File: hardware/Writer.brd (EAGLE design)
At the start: 54 x 56 mm, 52 parts, among them CN1 ZX62-B-5PA(11), CN2 TTL-232R-3V3, CN3 WiFi-Header, CN4 SOCKET-HEADER-7614-5002, IC1 ATMEGA32U4AU

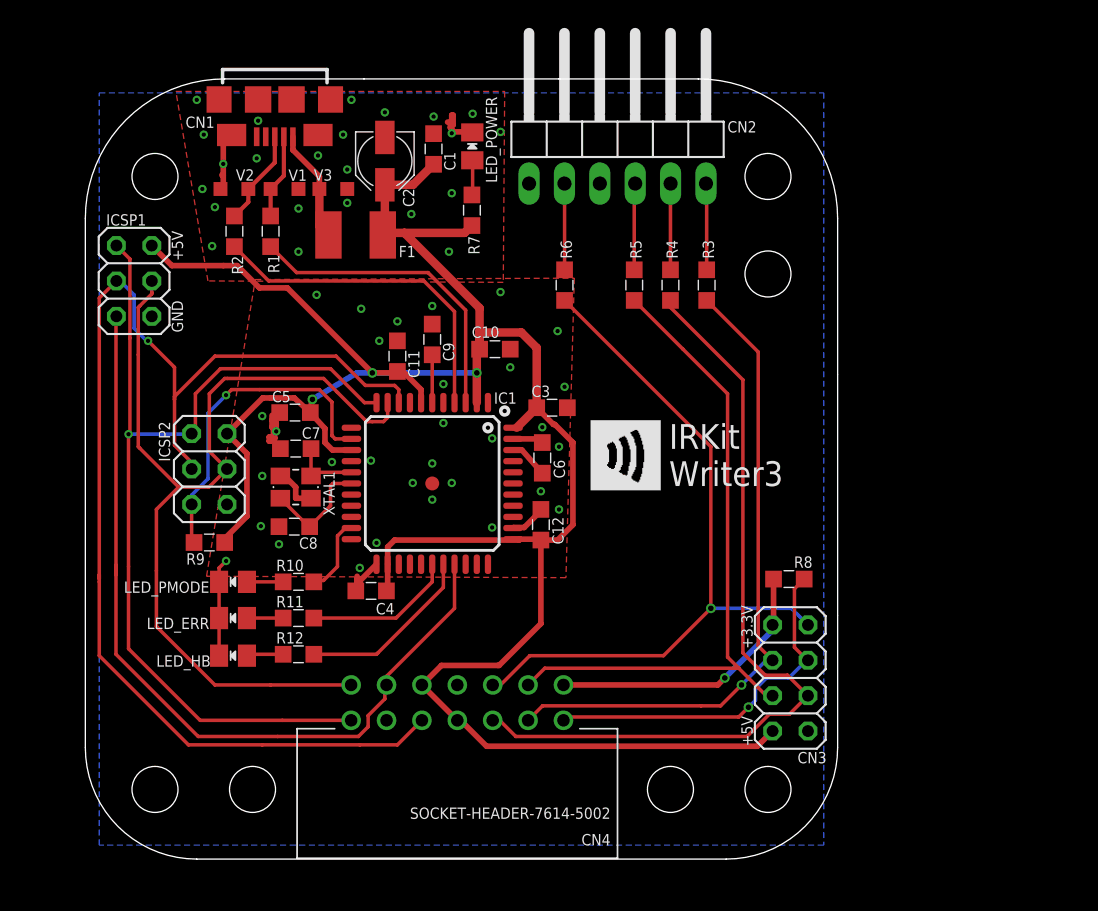
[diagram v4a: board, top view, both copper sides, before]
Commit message: make holes for IRKit ICSP and Wi-Fi header larger to fit pogopin diameter 1.02mm
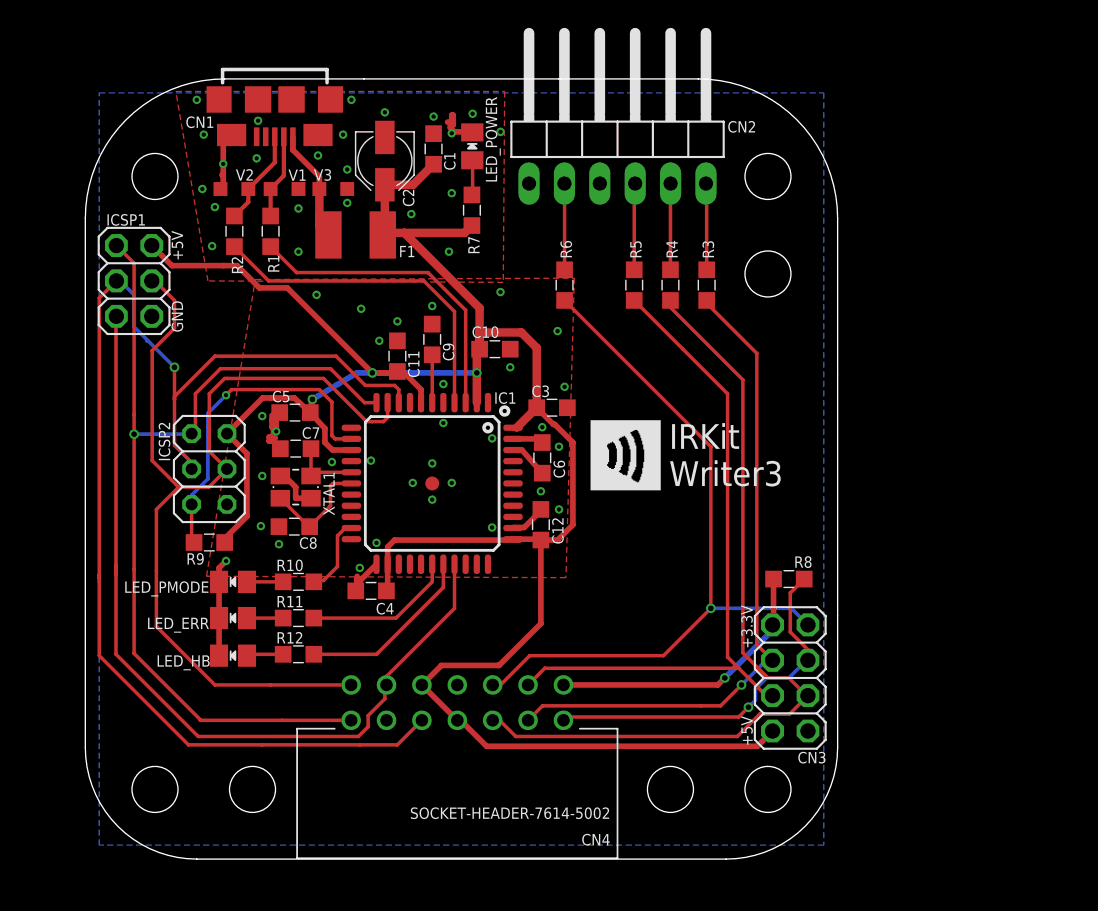
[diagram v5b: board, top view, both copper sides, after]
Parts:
- CN3: device my:2X04 -> my:2X04/D1.1
- ICSP1: device my:2X03 -> my:2X03/D1.1
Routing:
- net IRKIT/MOSI: track 68.6 -> 69.2 mm
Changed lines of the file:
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@@
 <element name="STANDOFF2" library="my" package="STAND-OFF" value="STAND-OFF" x="5" y="5" smashed="yes"/>
 <element name="STANDOFF4" library="my" package="STAND-OFF" value="STAND-OFF" x="5" y="49" smashed="yes"/>
-<element name="ICSP1" library="my" package="2X03" value="IRKit ICSP" x="3.5" y="41.5" smashed="yes" rot="R270">
+<element name="ICSP1" library="my" package="2X03/D1.1" value="IRKit ICSP" x="3.5" y="41.5" smashed="yes" rot="R270">
 <attribute name="NAME" x="1.49" y="45.475" size="0.8128" layer="25" ratio="10"/>
 <attribute name="VALUE" x="-0.945" y="45.31" size="0.8128" layer="27" rot="R270"/>
@@
 <attribute name="VALUE" x="17.495" y="41.625" size="1.27" layer="27"/>
 </element>
-<element name="CN3" library="my" package="2X04" value="WiFi-Header" x="50.6" y="13" smashed="yes" rot="R270">
+<element name="CN3" library="my" package="2X04/D1.1" value="WiFi-Header" x="50.6" y="13" smashed="yes" rot="R270">
 <attribute name="NAME" x="51.12" y="6.875" size="0.8128" layer="25" ratio="10"/>
 <attribute name="VALUE" x="46.155" y="18.08" size="1.27" layer="27" rot="R270"/>
@@
 <contactref element="LED_ERR" pad="K"/>
 <contactref element="LED_HB" pad="K"/>
-<wire x1="9.6" y1="19.9" x2="9.6" y2="17.3" width="0.254" layer="1"/>
+<wire x1="9.6" y1="19.9" x2="9.6" y2="17.3" width="0.4064" layer="1"/>
 <wire x1="9.6" y1="20.1" x2="9.6" y2="19.9" width="0.4064" layer="1"/>
-<wire x1="9.6" y1="17.1" x2="9.6" y2="14.6" width="0.254" layer="1"/>
+<wire x1="9.6" y1="17.1" x2="9.6" y2="14.6" width="0.4064" layer="1"/>
 <wire x1="9.6" y1="17.1" x2="9.6" y2="17.3" width="0.4064" layer="1"/>
 <via x="13.9" y="22.6" extent="1-16" drill="0.3048"/>
-<wire x1="9.6" y1="20.1" x2="9.6" y2="20.9" width="0.254" layer="1"/>
-<wire x1="9.6" y1="20.9" x2="10.1" y2="21.4" width="0.254" layer="1"/>
+<wire x1="9.6" y1="20.1" x2="9.6" y2="20.9" width="0.4064" layer="1"/>
+<wire x1="9.6" y1="20.9" x2="10.1" y2="21.4" width="0.4064" layer="1"/>
 </signal>
 <signal name="+3V3" class="4">
@@
 <contactref element="R8" pad="1"/>
 <wire x1="50.9" y1="19.4" x2="51.6" y2="20.1" width="0.254" layer="1"/>
-<wire x1="50.9" y1="15.2" x2="50.9" y2="19.4" width="0.254" layer="1"/>
-<wire x1="51.8" y1="14.3" x2="50.9" y2="15.2" width="0.254" layer="1"/>
 <wire x1="51.8" y1="14.3" x2="51.87" y2="14.27" width="0.254" layer="1"/>
 <contactref element="CN4" pad="1"/>
@@
 <wire x1="47.6" y1="10.9" x2="48.1" y2="11.4" width="0.254" layer="16"/>
 <wire x1="48.1" y1="11.4" x2="48.1" y2="12.2" width="0.254" layer="16"/>
+<wire x1="50.9" y1="19.4" x2="50.6" y2="19.1" width="0.254" layer="1"/>
+<wire x1="50.6" y1="19.1" x2="50.6" y2="16.3" width="0.254" layer="1"/>
+<wire x1="50.6" y1="16.3" x2="51.87" y2="15.03" width="0.254" layer="1"/>
+<wire x1="51.87" y1="15.03" x2="51.87" y2="14.27" width="0.254" layer="1"/>
 </signal>
 <signal name="WIFI_UART0_CTS">
 <contactref element="CN3" pad="3"/>
 <contactref element="R3" pad="2"/>
-<wire x1="48.3" y1="36.4" x2="44.6" y2="40.1" width="0.254" layer="1"/>
-<wire x1="48.3" y1="15.3" x2="48.3" y2="36.4" width="0.254" layer="1"/>
-<wire x1="49.3" y1="14.3" x2="48.3" y2="15.3" width="0.254" layer="1"/>
 <wire x1="49.3" y1="14.3" x2="49.33" y2="14.27" width="0.254" layer="1"/>
 <contactref element="CN4" pad="3"/>
@@
 <wire x1="47.1" y1="12.5" x2="48.87" y2="14.27" width="0.254" layer="16"/>
 <wire x1="48.87" y1="14.27" x2="49.33" y2="14.27" width="0.254" layer="16"/>
+<wire x1="49.3" y1="14.3" x2="48.2" y2="15.4" width="0.254" layer="1"/>
+<wire x1="48.2" y1="15.4" x2="48.2" y2="36.3" width="0.254" layer="1"/>
+<wire x1="48.2" y1="36.3" x2="44.6" y2="39.9" width="0.254" layer="1"/>
+<wire x1="44.6" y1="39.9" x2="44.6" y2="40.1" width="0.254" layer="1"/>
 </signal>
 <signal name="WIFI_UART0_RX">
@@
 <contactref element="R4" pad="2"/>
 <contactref element="CN4" pad="5"/>
-<wire x1="51.87" y1="11.73" x2="50.4" y2="13.2" width="0.254" layer="1"/>
-<wire x1="50.4" y1="13.2" x2="48.8" y2="13.2" width="0.254" layer="1"/>
-<wire x1="48.8" y1="13.2" x2="47.2" y2="14.8" width="0.254" layer="1"/>
 <wire x1="47.2" y1="14.8" x2="47.2" y2="34.4" width="0.254" layer="1"/>
 <wire x1="47.2" y1="34.4" x2="42" y2="39.6" width="0.254" layer="1"/>
 <wire x1="42" y1="39.6" x2="42" y2="40.1" width="0.254" layer="1"/>
 <wire x1="51.87" y1="11.73" x2="50.54" y2="10.4" width="0.254" layer="1"/>
-<wire x1="50.54" y1="10.4" x2="49.1" y2="10.4" width="0.254" layer="1"/>
-<wire x1="49.1" y1="10.4" x2="47.5" y2="8.8" width="0.254" layer="1"/>
-<wire x1="47.5" y1="8.8" x2="30.9" y2="8.8" width="0.254" layer="1"/>
 <wire x1="30.9" y1="8.8" x2="29.74" y2="9.96" width="0.254" layer="1"/>
 <wire x1="29.74" y1="9.96" x2="29.24" y2="9.96" width="0.254" layer="1"/>
+<wire x1="30.9" y1="8.8" x2="46.8" y2="8.8" width="0.254" layer="1"/>
+<wire x1="46.8" y1="8.8" x2="48.4" y2="10.4" width="0.254" layer="1"/>
+<wire x1="48.4" y1="10.4" x2="50.54" y2="10.4" width="0.254" layer="1"/>
+<wire x1="47.2" y1="14.8" x2="49" y2="13" width="0.254" layer="1"/>
+<wire x1="49" y1="13" x2="50.5" y2="13" width="0.254" layer="1"/>
+<wire x1="50.5" y1="13" x2="51.77" y2="11.73" width="0.254" layer="1"/>
+<wire x1="51.77" y1="11.73" x2="51.87" y2="11.73" width="0.254" layer="1"/>
 </signal>
 <signal name="UCAP">
@@
 <wire x1="7.9" y1="33.4" x2="7.9" y2="30.81" width="0.254" layer="1"/>
 <wire x1="7.9" y1="30.81" x2="7.63" y2="30.54" width="0.254" layer="1"/>
-<wire x1="2.23" y1="44.04" x2="3.2" y2="43.07" width="0.254" layer="1"/>
-<wire x1="3.2" y1="43.07" x2="3.2" y2="37.4" width="0.254" layer="1"/>
 <wire x1="7.63" y1="30.54" x2="7.59" y2="30.5" width="0.254" layer="16"/>
-<wire x1="7.59" y1="30.5" x2="3.1" y2="30.5" width="0.254" layer="16"/>
-<via x="3.1" y="30.5" extent="1-16" drill="0.3048"/>
-<wire x1="3.1" y1="30.5" x2="3.2" y2="30.6" width="0.254" layer="1"/>
-<wire x1="3.2" y1="30.6" x2="3.2" y2="37.4" width="0.254" layer="1"/>
-<wire x1="3.1" y1="21" x2="3.1" y2="30.5" width="0.254" layer="1"/>
-<wire x1="14.14" y1="9.96" x2="8.24" y2="9.96" width="0.254" layer="1"/>
-<wire x1="8.24" y1="9.96" x2="3.1" y2="15.1" width="0.254" layer="1"/>
-<wire x1="3.1" y1="15.1" x2="3.1" y2="21" width="0.254" layer="1"/>
+<wire x1="14.14" y1="9.96" x2="8.3" y2="9.96" width="0.254" layer="1"/>
+<wire x1="8.3" y1="9.96" x2="8.24" y2="9.96" width="0.254" layer="1"/>
+<wire x1="2.23" y1="44.04" x2="3.5" y2="42.77" width="0.254" layer="1"/>
+<wire x1="3.5" y1="42.77" x2="3.5" y2="31.9" width="0.254" layer="1"/>
+<wire x1="3.5" y1="31.9" x2="3.5" y2="30.5" width="0.254" layer="1"/>
+<wire x1="3.5" y1="30.5" x2="3.5" y2="20.8" width="0.254" layer="1"/>
+<wire x1="3.5" y1="20.8" x2="3.5" y2="14.76" width="0.254" layer="1"/>
+<wire x1="3.5" y1="14.76" x2="8.3" y2="9.96" width="0.254" layer="1"/>
+<wire x1="7.59" y1="30.5" x2="3.5" y2="30.5" width="0.254" layer="16"/>
+<via x="3.5" y="30.5" extent="1-16" drill="0.4"/>
 </signal>
 <signal name="IRKIT/SCK">
@@
 <wire x1="7.63" y1="28" x2="7.63" y2="28.47" width="0.254" layer="1"/>
 <wire x1="2.5" y1="41.5" x2="3.5" y2="40.5" width="0.254" layer="16"/>
-<wire x1="3.5" y1="40.5" x2="3.5" y2="38.1" width="0.254" layer="16"/>
-<wire x1="3.5" y1="38.1" x2="4.4" y2="37.2" width="0.254" layer="16"/>
 <wire x1="4.4" y1="37.2" x2="4.5" y2="37.2" width="0.254" layer="16"/>
-<via x="4.5" y="37.2" extent="1-16" drill="0.3048"/>
-<wire x1="4.5" y1="37.2" x2="6.4" y2="35.3" width="0.254" layer="1"/>
 <wire x1="6.4" y1="35.3" x2="6.4" y2="33" width="0.254" layer="1"/>
 <wire x1="2.3" y1="41.5" x2="2.4" y2="41.5" width="0.254" layer="16"/>
@@
 <wire x1="7.4" y1="8.2" x2="1" y2="14.6" width="0.254" layer="1"/>
 <wire x1="1" y1="14.6" x2="1" y2="19.9" width="0.254" layer="1"/>
+<via x="6.4" y="35.3" extent="1-16" drill="0.4"/>
+<wire x1="6.4" y1="35.3" x2="3.5" y2="38.2" width="0.254" layer="16"/>
+<wire x1="3.5" y1="38.2" x2="3.5" y2="40.5" width="0.254" layer="16"/>
+<wire x1="3.5" y1="38.2" x2="4.4" y2="37.2" width="0" layer="19" extent="16-16"/>
 </signal>
 <signal name="IRKIT/!RESET">
@@
 <wire x1="21.7" y1="31.7" x2="21.4" y2="31.4" width="0.254" layer="1"/>
 <wire x1="21.4" y1="31.4" x2="20.6" y2="31.4" width="0.254" layer="1"/>
-<wire x1="4.77" y1="41.5" x2="4.77" y2="41.03" width="0.254" layer="1"/>
 <wire x1="20.6" y1="31.4" x2="20.2" y2="31.4" width="0.254" layer="1"/>
 <wire x1="20.2" y1="31.4" x2="18.1" y2="33.5" width="0.254" layer="1"/>
@@
 <wire x1="8.9" y1="33.4" x2="8.9" y2="29.27" width="0.254" layer="1"/>
 <wire x1="8.9" y1="29.27" x2="10.17" y2="28" width="0.254" layer="1"/>
-<wire x1="4.77" y1="41.03" x2="4.77" y2="40.67" width="0.254" layer="1"/>
-<wire x1="4.77" y1="40.67" x2="4.77" y2="40.57" width="0.254" layer="1"/>
-<wire x1="4.77" y1="40.57" x2="3.9" y2="39.7" width="0.254" layer="1"/>
-<wire x1="3.9" y1="29.5" x2="6.7" y2="26.7" width="0.254" layer="1"/>
-<wire x1="3.9" y1="39.7" x2="3.8" y2="39.6" width="0.254" layer="1"/>
-<wire x1="3.8" y1="39.6" x2="3.8" y2="36.2" width="0.254" layer="1"/>
-<wire x1="3.8" y1="36.2" x2="3.8" y2="29.6" width="0.254" layer="1"/>
-<wire x1="3.8" y1="29.6" x2="3.9" y2="29.5" width="0.254" layer="1"/>
 <wire x1="13.3" y1="12.5" x2="9.3" y2="12.5" width="0.254" layer="1"/>
 <wire x1="9.3" y1="12.5" x2="5.2" y2="16.6" width="0.254" layer="1"/>
 <wire x1="5.2" y1="16.6" x2="5.1" y2="16.7" width="0.254" layer="1"/>
 <wire x1="5.1" y1="16.7" x2="5.1" y2="20.7" width="0.254" layer="1"/>
+<wire x1="6.7" y1="26.7" x2="4.8" y2="28.6" width="0.254" layer="1"/>
+<wire x1="4.8" y1="28.6" x2="4.8" y2="36.5" width="0.254" layer="1"/>
+<wire x1="4.8" y1="36.5" x2="6.4" y2="38.1" width="0.254" layer="1"/>
+<wire x1="6.4" y1="38.1" x2="6.4" y2="40.1" width="0.254" layer="1"/>
+<wire x1="6.4" y1="40.1" x2="5" y2="41.5" width="0.254" layer="1"/>
+<wire x1="5" y1="41.5" x2="4.77" y2="41.5" width="0.254" layer="1"/>
 </signal>
 <signal name="N$1">
